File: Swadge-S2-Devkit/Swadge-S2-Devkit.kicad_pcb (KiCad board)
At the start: 2 copper layers, 99.9 x 99.9 mm, 83 parts, among them J1 USB_B_Micro, J2 DEBUG_BANK_C, J3 DEBUG_BANK_B, J4 DEBUG_BANK_A, J5 MICSEL, J6 TRYMIC, M1 Motor_DC, Q1 Q_N_FET, Q2 AP2003_PN_FET, Q3 AP2003_PN_FET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

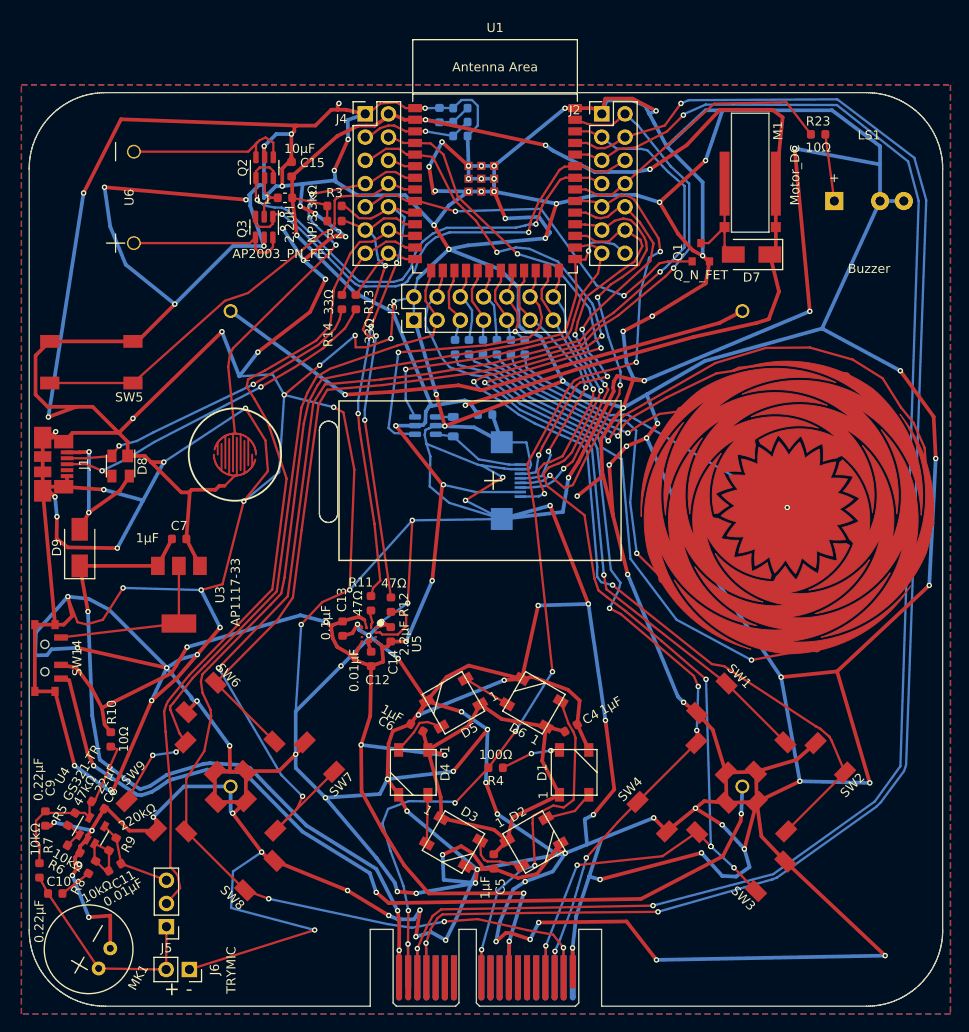
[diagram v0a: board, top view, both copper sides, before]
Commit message: Ripped all traces, adjusted part placement
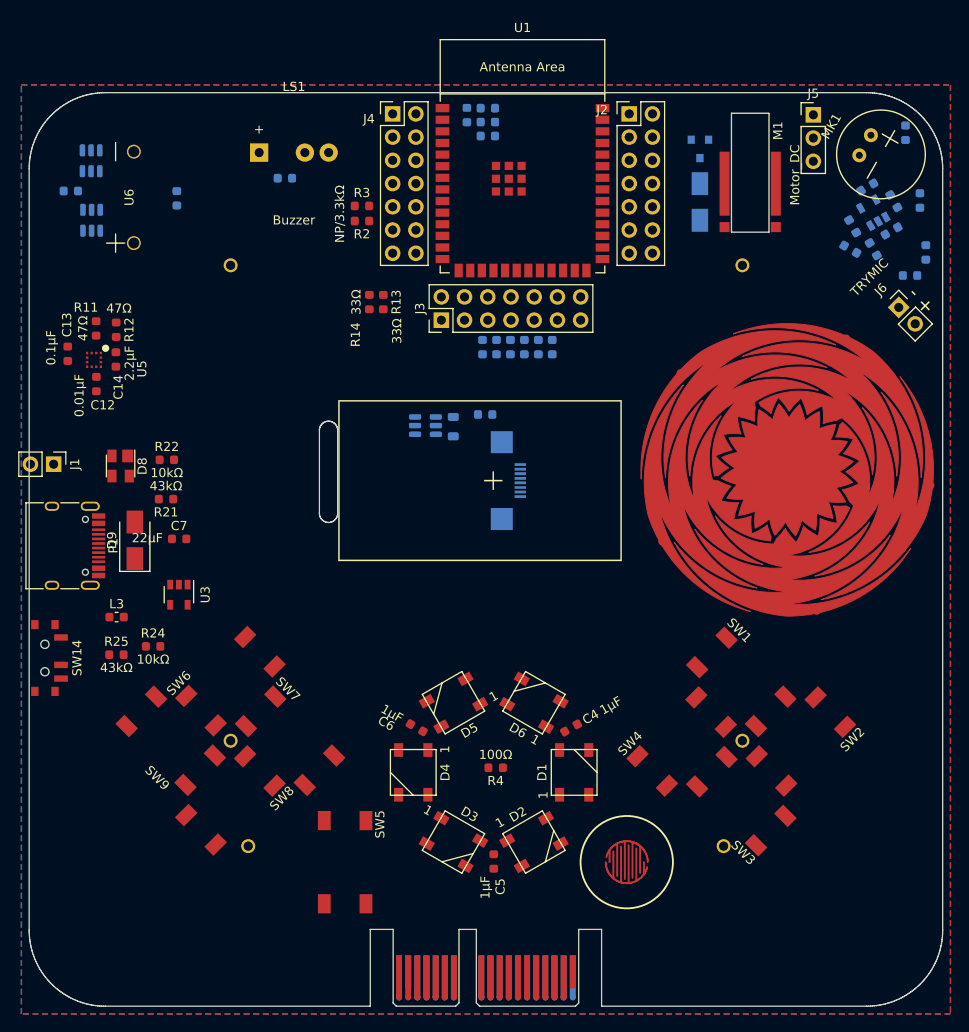
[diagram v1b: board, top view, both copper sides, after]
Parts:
- added BT3: Battery, Swadge_Parts:2460, B.Cu at (152.4, 134.0)
- added L3: 2.2uH, Swadge_Parts:L_0603_1608Metric, F.Cu at (112.0, 109.0)
- added P1: USB_C_Plug_USB2.0, Swadge_Parts:USB_C_Receptacle_HRO_TYPE-C-31-M-12, F.Cu at (106.0, 101.2)
- added R21: 43kΩ, Swadge_Parts:R_0603_1608Metric, F.Cu at (117.4, 96.1)
- added R22: 10kΩ, Swadge_Parts:R_0603_1608Metric, F.Cu at (117.5, 91.8)
- added R24: 10kΩ, Swadge_Parts:R_0603_1608Metric, F.Cu at (116.0, 112.2)
- added R25: 43kΩ, Swadge_Parts:R_0603_1608Metric, F.Cu at (112.0, 113.1)
- C10, C11, C15, C8, C9, D7, L1, Q1, Q2, Q3, R10, R23, R5, R6, R7, R8, R9, U4: moved to B.Cu
- C7: value 1μF -> 22μF
- J1: value USB_B_Micro -> CurrentMonitor; footprint Swadge_Parts:USB_Micro-B_Molex_47346-0001 -> Swadge_Parts:PinHeader_1x02_P2.54mm_Vertical
- U3: value AP1117-33 -> MT3410; footprint Swadge_Parts:SOT-223-3_TabPin2 -> Swadge_Parts:SOT-23-5
- moved MK1 122.7 mm to (195.6, 58.4), turned to -120 degrees
- moved R7 118.2 mm to (200.5, 69.1)
- moved C9 117.1 mm to (199.9, 63.4)
- moved C10 115.4 mm to (198.8, 71.6), turned to 0 degrees
- moved J5 113.5 mm to (188.2, 54.1), turned to 0 degrees
- moved R5 112.5 mm to (197.0, 63.5), turned to 120 degrees
- moved R6 112.1 mm to (196.8, 66.8), turned to 30 degrees
- moved R10 109.3 mm to (198.3, 56.0)
- moved R8 108.9 mm to (194.8, 68.8), turned to -60 degrees
- moved U4 108.9 mm to (194.8, 64.8), turned to 120 degrees
- moved C8 107.9 mm to (194.1, 62.0), turned to 30 degrees
- moved J6 106.1 mm to (197.5, 75.1), turned to 45 degrees
- moved R9 105.4 mm to (192.5, 66.3), turned to -60 degrees
- moved C11 105.1 mm to (192.3, 68.8), turned to -30 degrees
- moved LS1 63.1 mm to (127.6, 58.2)
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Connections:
- BT2 pad 1: BATTPLUS -> BATTMID2
- C7 pad 1: +5V -> Net-(SW14-Pad2)
- J1 pad 1: 5VIN -> Net-(SW14-Pad1)
- J1 pad 2: Net-(D8-Pad2) -> +5V
- J3 pad 10: TOUCH_6 -> TFT_RESET
- J3 pad 5: TOUCH_1 -> unconnected-(J3-Pad5)
- J3 pad 6: TOUCH_2 -> unconnected-(J3-Pad6)
- J3 pad 7: TOUCH_3 -> unconnected-(J3-Pad7)
- J3 pad 8: TOUCH_4 -> unconnected-(J3-Pad8)
- J3 pad 9: TOUCH_5 -> unconnected-(J3-Pad9)
- R13 pad 2: Net-(D8-Pad3) -> Net-(D8-Pad2)
- R14 pad 2: Net-(D8-Pad2) -> Net-(D8-Pad3)
- SW14 pad 2: +3V3 -> Net-(SW14-Pad2)
- U3 pad 1: GND -> Net-(SW14-Pad2)
- U3 pad 2: Net-(SW14-Pad1) -> GND
- U3 pad 3: +5V -> Net-(L3-Pad2)
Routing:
- net GND: track 1864.0 -> 0.00 mm, vias 153 -> 0
- net +3V3: track 380.6 -> 0.00 mm, vias 15 -> 0
- net TX: track 174.9 -> 0.00 mm, vias 3 -> 0
- net RX: track 173.3 -> 0.00 mm, vias 3 -> 0
- net BTN_8: track 153.2 -> 0.00 mm, vias 4 -> 0
- net BTN_7: track 130.0 -> 0.00 mm, vias 3 -> 0
- net BTN_2: track 125.0 -> 0.00 mm, vias 4 -> 0
- net BTN_3: track 118.5 -> 0.00 mm, vias 7 -> 0
- net LED: track 114.3 -> 0.00 mm, vias 7 -> 0
- net BTN_6: track 112.6 -> 0.00 mm, vias 1 -> 0
- net BTN_4: track 108.7 -> 0.00 mm, vias 5 -> 0
- net BTN_1: track 103.5 -> 0.00 mm, vias 4 -> 0
- net BATTPLUS: track 96.2 -> 0.00 mm, vias 3 -> 0
- net MIC: track 91.2 -> 0.00 mm
- net +5V: track 84.4 -> 0.00 mm, vias 3 -> 0
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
